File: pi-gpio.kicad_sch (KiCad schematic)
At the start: 15 parts, among them J1 Raspberry_Pi_2_3, J2 printerRelay, J3 UART, J4 uartPower, J5 adxl, J6 powerIn

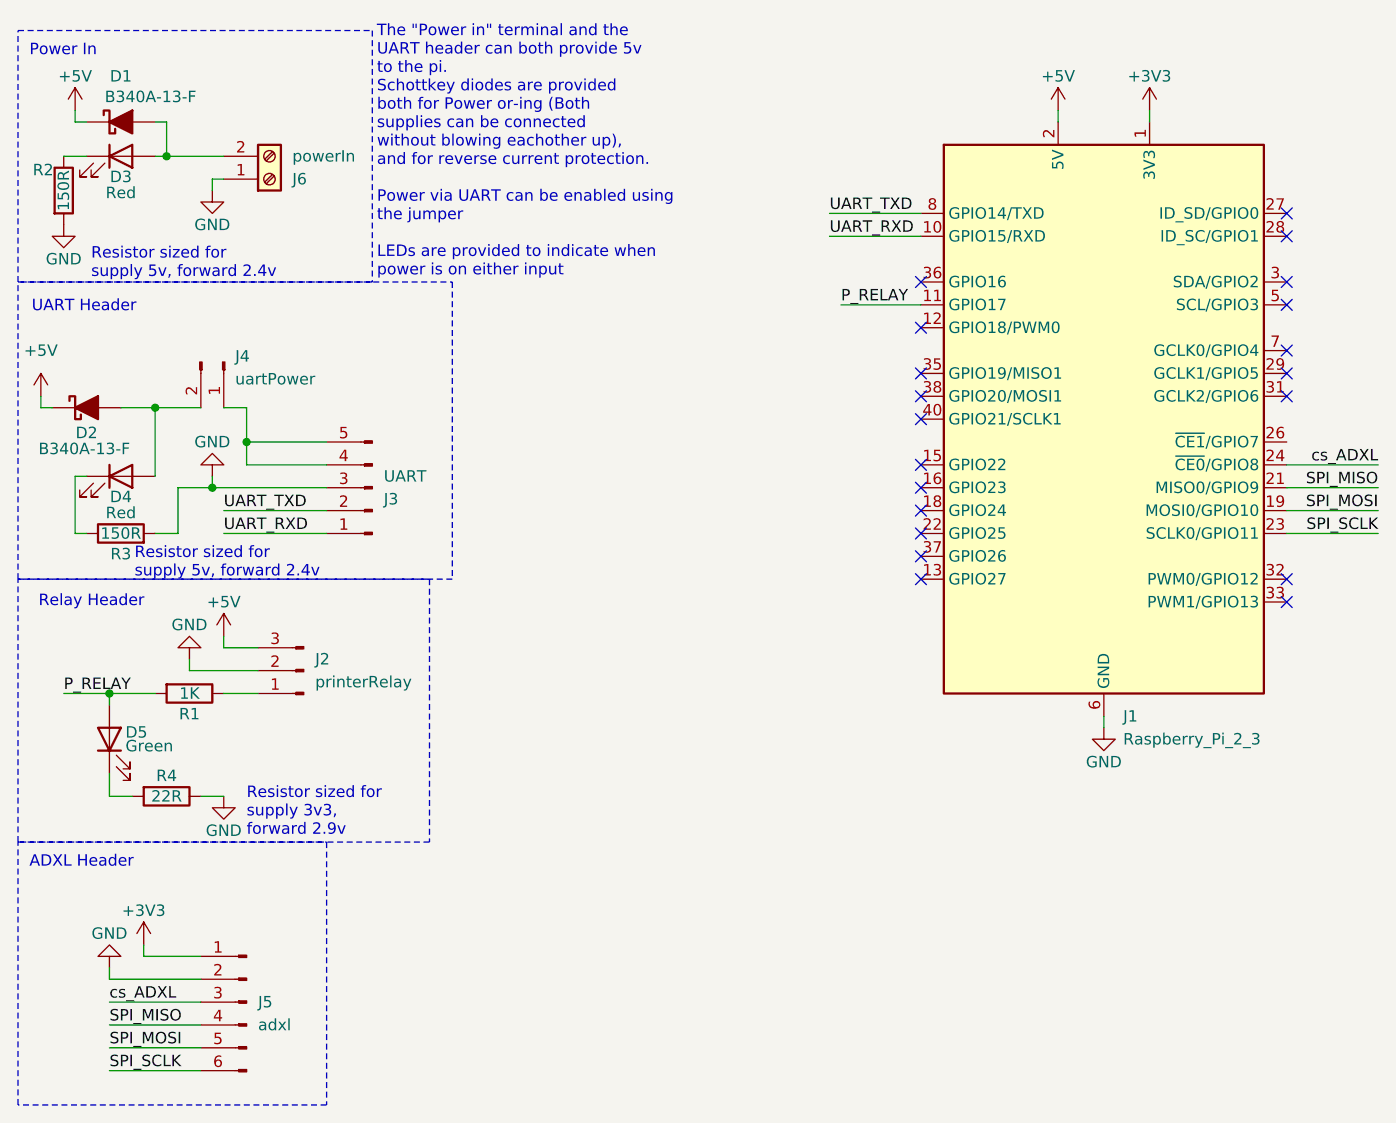
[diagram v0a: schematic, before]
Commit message: Doubled SPI headers, added I2C
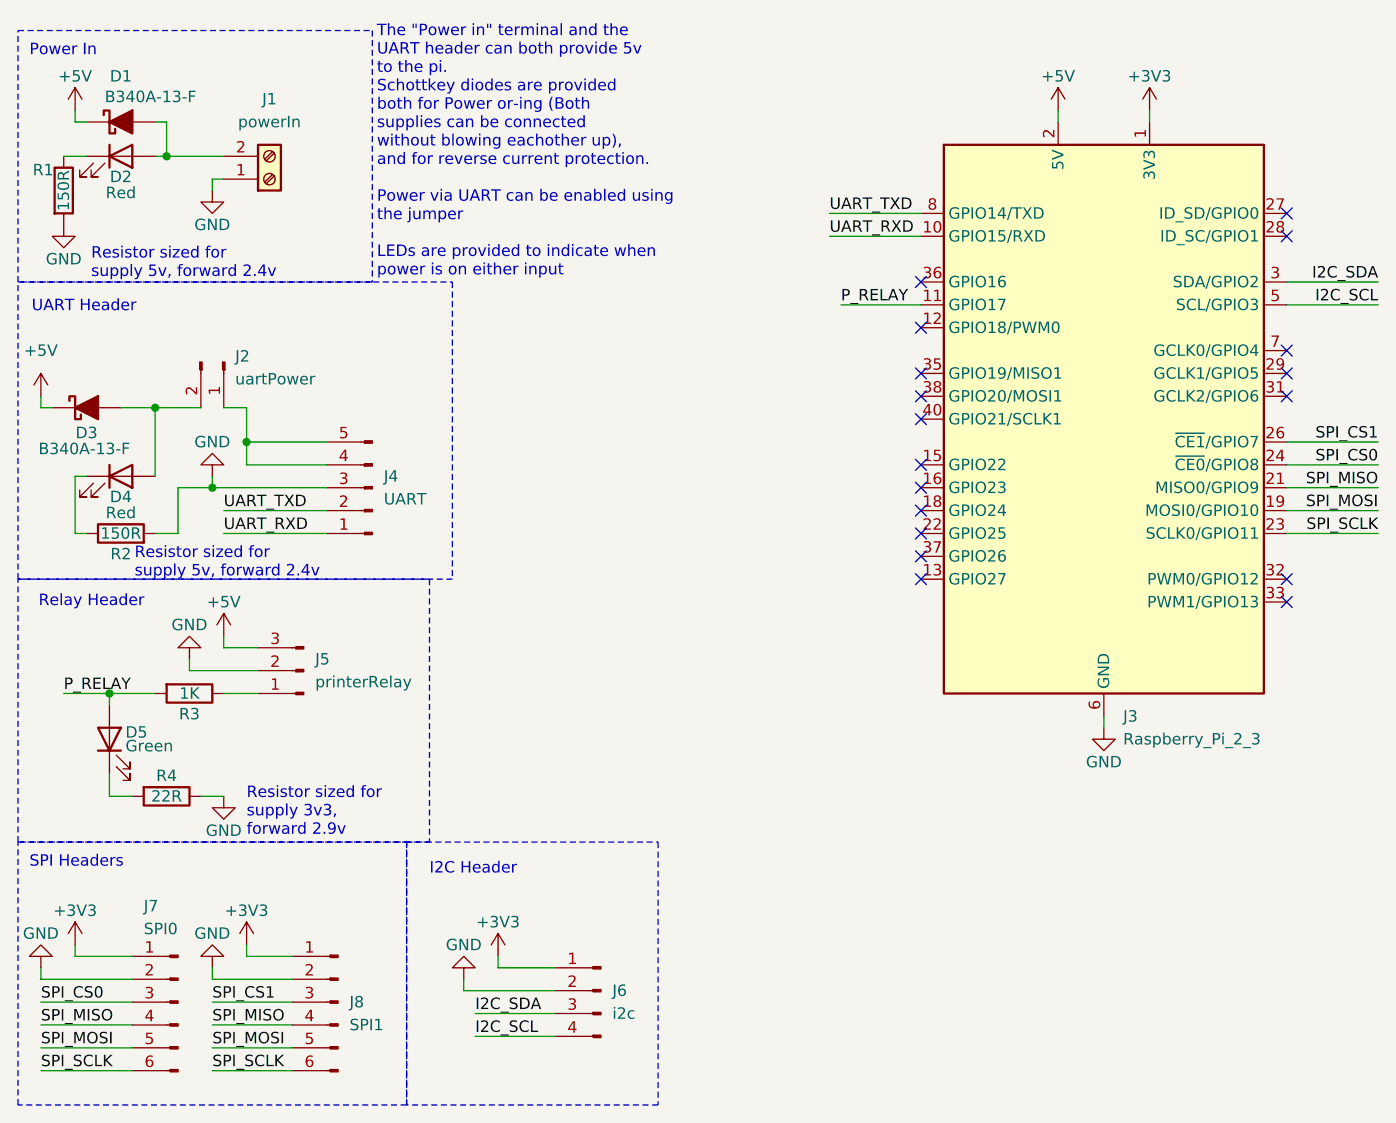
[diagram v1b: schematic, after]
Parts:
- added J6: i2c, Connector_JST:JST_XH_B4B-XH-A_1x04_P2.50mm_Vertical, symbol Connector:Conn_01x04_Pin
- added J8: SPI1, Connector_JST:JST_PH_B6B-PH-K_1x06_P2.00mm_Vertical, symbol Connector:Conn_01x06_Pin
- J7: renamed from J5; value adxl -> SPI0; footprint Connector_PinHeader_2.54mm:PinHeader_1x06_P2.54mm_Vertical -> Connector_JST:JST_PH_B6B-PH-K_1x06_P2.00mm_Vertical
- renumbered D3 to D2, D2 to D3, J6 to J1, J4 to J2, J1 to J3, J3 to J4, J2 to J5, R2 to R1, R3 to R2, R1 to R3
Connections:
- net +3V3: now also J6.1 (Pin_1), J8.1 (Pin_1)
- net GND: now also J6.2 (Pin_2), J8.2 (Pin_2)
- net SPI_MISO: now also J8.4 (Pin_4)
- net SPI_MOSI: now also J8.5 (Pin_5)
- net SPI_SCLK: now also J8.6 (Pin_6)
- net SPI_CS1: now reaches J3.26 (~{CE1}/GPIO7)
- net SPI_CS1: now also J8.3 (Pin_3)
- net I2C_SDA: now reaches J3.3 (SDA/GPIO2)
- net I2C_SDA: now also J6.3 (Pin_3)
- net I2C_SCL: now reaches J3.5 (SCL/GPIO3)
- net I2C_SCL: now also J6.4 (Pin_4)
- net cs_ADXL renamed SPI_CS0
- no-connect marks 20 -> 18
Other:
- note added: "I2C Header"
- note added: "SPI Headers"
- note removed: "ADXL Header"
- moved on the sheet: J7

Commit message: Added readme
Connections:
- net +3V3: now also J6.4 (Pin_4); no longer J6.1 (Pin_1)
- net GND: now also J6.3 (Pin_3); no longer J6.2 (Pin_2)
- net I2C_SCL: now also J6.1 (Pin_1); no longer J6.4 (Pin_4)
- net I2C_SDA: now also J6.2 (Pin_2); no longer J6.3 (Pin_3)
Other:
- moved on the sheet: J6
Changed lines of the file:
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@@
 	(symbol
 		(lib_id "Connector:Conn_01x04_Pin")
-		(at 80.01 121.92 0)
-		(mirror y)
+		(at 80.01 124.46 180)
 		(unit 1)
 		(exclude_from_sim no)
@@
 		)
 		(property "Footprint" "Connector_JST:JST_XH_B4B-XH-A_1x04_P2.50mm_Vertical"
-			(at 80.01 121.92 0)
+			(at 80.01 124.46 0)
 			(effects
 				(font
@@
 		)
 		(property "Datasheet" "~"
-			(at 80.01 121.92 0)
+			(at 80.01 124.46 0)
 			(effects
 				(font
@@
 		)
 		(property "Description" "Generic connector, single row, 01x04, script generated"
-			(at 80.01 121.92 0)
+			(at 80.01 124.46 0)
 			(effects
 				(font
